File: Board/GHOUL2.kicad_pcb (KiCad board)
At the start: 2 copper layers, 106.7 x 73.7 mm, 16 parts, among them J1 Conn_01x02, Q1 IRF540N, Q2 IRF540N, U1 Teensy3.5_All_Pins, U10 GHOULIMU, U2 LM7805_TO220, U3 BMP280, U4 Feedback_Serv, U5 LM1084-ADJ, U6 NichromeConnector, U7 Ultimate_GPS_Breakout_v3, U8 Xbee, U9 NichromeConnector

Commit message: sometimes the fastest way to get to the end is to throw everything out and start over
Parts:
- R1, U5: moved to F.Cu
- moved Q2 33.7 mm to (189.7, 91.2), turned to 0 degrees
- moved U6 18.8 mm to (195.8, 106.4), turned to 90 degrees
- moved C1 16.1 mm to (165.0, 68.7), turned to 180 degrees
- moved R1 15.3 mm to (181.3, 116.8), turned to 180 degrees
- moved U5 15.3 mm to (181.3, 104.1), turned to 180 degrees
- moved U2 12.4 mm to (176.2, 77.9), turned to -90 degrees
- moved U4 10.2 mm to (105.5, 76.1)
- moved U1 8.03 mm to (160.0, 106.7)
- moved U9 7.16 mm to (195.8, 116.6), turned to -90 degrees
- moved Q1 6.61 mm to (189.7, 129.3), turned to 0 degrees
- moved BT1 3.59 mm to (139.7, 129.5)
- moved U8 3.59 mm to (128.8, 135.8)
- moved J1 2.71 mm to (185.8, 73.7)
- moved U7 2.54 mm to (128.7, 104.0)
- moved U10 2.54 mm to (148.5, 91.3)
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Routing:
- net GND: track 235.9 -> 0.00 mm, vias 3 -> 0
- net 5v pwr: track 182.4 -> 8.24 mm, vias 1 -> 0
- net Net-(U1-Pad22): track 73.0 -> 0.00 mm
- net Nic2: track 68.7 -> 0.00 mm, vias 1 -> 0
- net Net-(U1-Pad2): track 67.0 -> 0.00 mm
- net Net-(U1-Pad3): track 57.7 -> 0.00 mm
- net Nic1: track 51.6 -> 0.00 mm
- net Feedback: track 50.1 -> 0.00 mm
- net Net-(U1-Pad12): track 48.9 -> 0.00 mm
- net Net-(U1-Pad51): track 44.9 -> 0.00 mm, vias 1 -> 0
- net Net-(U1-Pad9): track 41.5 -> 0.00 mm
- net Net-(U1-Pad10): track 34.6 -> 0.00 mm
- net Vin: track 29.0 -> 60.9 mm, vias 0 -> 5
- net Net-(U1-Pad11): track 27.4 -> 0.00 mm
- net Net-(BT1-Pad1): track 14.8 -> 0.00 mm
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- removed copper zone on F.Cu, net GND
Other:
- board size 106.7 x 73.7 mm -> 105.1 x 68.6 mm

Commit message: fixed some routing
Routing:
- net Net-(R1-Pad1): track 30.3 -> 36.1 mm
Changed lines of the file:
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@@
   (segment (start 195.81 103.905) (end 195.81 93.975) (width 2) (layer "F.Cu") (net 24))
   (segment (start 195.81 93.975) (end 193.04 91.205) (width 0.25) (layer "F.Cu") (net 24))
+  (segment (start 189.84 116.605) (end 195.81 116.605) (width 2) (layer "F.Cu") (net 25))
   (segment (start 195.81 110.635) (end 195.81 106.405) (width 2) (layer "F.Cu") (net 25))
   (segment (start 195.58 116.605) (end 195.81 116.605) (width 2) (layer "F.Cu") (net 25))
-  (segment (start 192.71 113.735) (end 195.58 116.605) (width 2) (layer "F.Cu") (net 25))
   (segment (start 187.065 106.68) (end 187.065 108.09) (width 2) (layer "F.Cu") (net 25))
   (segment (start 187.065 108.09) (end 192.71 113.735) (width 2) (layer "F.Cu") (net 25))
+  (segment (start 187.065 119.38) (end 192.71 113.735) (width 2) (layer "F.Cu") (net 25))
+  (segment (start 187.065 119.38) (end 189.84 116.605) (width 2) (layer "F.Cu") (net 25))
   (segment (start 192.71 113.735) (end 195.81 110.635) (width 2) (layer "F.Cu") (net 25))
-  (segment (start 187.065 119.38) (end 192.71 113.735) (width 2) (layer "F.Cu") (net 25))
   (segment (start 173.67 72.13) (end 172.98 72.13) (width 1) (layer "F.Cu") (net 45))
   (segment (start 172.98 72.13) (end 167.64 77.47) (width 1) (layer "F.Cu") (net 45))

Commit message: progress
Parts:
- moved U1 2.54 mm to (160.0, 104.1)
- moved U6 2.27 mm to (195.8, 104.1)
- moved U2 0.95 mm to (175.3, 77.9)
- moved U9 0.47 mm to (195.8, 117.1), turned to 90 degrees
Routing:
- net Vin: track 60.9 -> 88.7 mm, vias 5 -> 9
- net Net-(R1-Pad1): track 36.1 -> 33.0 mm
- net Net-(Q2-Pad2): track 13.8 -> 11.6 mm
- net 5v pwr: track 8.24 -> 6.39 mm
- net Net-(Q1-Pad2): track 11.7 -> 13.4 mm
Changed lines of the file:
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@@
   )
   (footprint "teensy:Teensy35_36_All_Pins" (layer "F.Cu")
-    (at 160.02 106.68 -90)
+    (at 160.02 104.14 -90)
     (property "Pinouts" "https://www.pjrc.com/teensy/pinout.html")
     (property "Sheetfile" "GHOUL2.kicad_sch")
@@
   )
   (footprint "Package_TO_SOT_SMD:TO-263-3_TabPin2" (layer "F.Cu")
-    (at 176.21 77.905 -90)
+    (at 175.26 77.905 -90)
     (descr "TO-263 / D2PAK / DDPAK SMD package, http://www.infineon.com/cms/en/product/packages/PG-TO263/PG-TO263-3-1/")
     (tags "D2PAK DDPAK TO-263 D2PAK-3 TO-263-3 SOT-404")
@@
   )
   (footprint "Connector_JST:JST_EH_B2B-EH-A_1x02_P2.50mm_Vertical" (layer "F.Cu")
-    (at 195.81 106.405 90)
+    (at 195.81 104.14 90)
     (descr "JST EH series connector, B2B-EH-A (http://www.jst-mfg.com/product/pdf/eng/eEH.pdf), generated with kicad-footprint-generator")
     (tags "connector JST EH vertical")
@@
   )
   (footprint "Connector_JST:JST_EH_B2B-EH-A_1x02_P2.50mm_Vertical" (layer "F.Cu")
-    (at 195.81 116.605 -90)
+    (at 195.81 117.075 90)
     (descr "JST EH series connector, B2B-EH-A (http://www.jst-mfg.com/product/pdf/eng/eEH.pdf), generated with kicad-footprint-generator")
     (tags "connector JST EH vertical")
@@
     (fp_line (start -2.5 -1.6) (end -2.5 2.2) (layer "F.Fab") (width 0.1))
     (fp_line (start -2.91 0.11) (end -2.91 2.61) (layer "F.Fab") (width 0.1))
-    (pad "1" thru_hole roundrect (at 0 0 270) (size 1.7 2) (drill 1) (layers *.Cu *.Mask) (roundrect_rratio 0.147059)
+    (pad "1" thru_hole oval (at 2.5 0 90) (size 1.7 2) (drill 1) (layers *.Cu *.Mask)
       (net 25 "Net-(R1-Pad1)") (pinfunction "In") (pintype "input"))
-    (pad "2" thru_hole oval (at 2.5 0 270) (size 1.7 2) (drill 1) (layers *.Cu *.Mask)
+    (pad "2" thru_hole roundrect (at 0 0 90) (size 1.7 2) (drill 1) (layers *.Cu *.Mask) (roundrect_rratio 0.147059)
       (net 16 "Net-(Q1-Pad2)") (pinfunction "Out") (pintype "input"))
     (model "${KICAD6_3DMODEL_DIR}/Connector_JST.3dshapes/JST_EH_B2B-EH-A_1x02_P2.50mm_Vertical.wrl"
@@
   (gr_line (start 93.98 137.16) (end 99.06 137.16) (layer "Edge.Cuts") (width 0.1))
   (gr_line (start 93.98 68.58) (end 93.98 137.16) (layer "Edge.Cuts") (width 0.1))
-  (segment (start 195.81 119.105) (end 195.81 126.53) (width 2) (layer "F.Cu") (net 16))
-  (segment (start 195.535 119.38) (end 195.81 119.105) (width 0.25) (layer "F.Cu") (net 16))
-  (segment (start 195.81 126.53) (end 193.035 129.305) (width 2) (layer "F.Cu") (net 16))
-  (segment (start 195.81 103.905) (end 195.81 93.975) (width 2) (layer "F.Cu") (net 24))
+  (segment (start 195.81 117.075) (end 193.035 119.85) (width 2) (layer "F.Cu") (net 16))
+  (segment (start 193.035 119.85) (end 193.035 129.305) (width 2) (layer "F.Cu") (net 16))
+  (segment (start 195.81 101.64) (end 195.81 93.975) (width 2) (layer "F.Cu") (net 24))
   (segment (start 195.81 93.975) (end 193.04 91.205) (width 0.25) (layer "F.Cu") (net 24))
-  (segment (start 189.84 116.605) (end 195.81 116.605) (width 2) (layer "F.Cu") (net 25))
-  (segment (start 195.81 110.635) (end 195.81 106.405) (width 2) (layer "F.Cu") (net 25))
-  (segment (start 195.58 116.605) (end 195.81 116.605) (width 2) (layer "F.Cu") (net 25))
-  (segment (start 187.065 106.68) (end 187.065 108.09) (width 2) (layer "F.Cu") (net 25))
-  (segment (start 187.065 108.09) (end 192.71 113.735) (width 2) (layer "F.Cu") (net 25))
-  (segment (start 187.065 119.38) (end 192.71 113.735) (width 2) (layer "F.Cu") (net 25))
-  (segment (start 187.065 119.38) (end 189.84 116.605) (width 2) (layer "F.Cu") (net 25))
+  (segment (start 187.065 119.38) (end 191.3225 115.1225) (width 2) (layer "F.Cu") (net 25))
+  (segment (start 195.81 110.635) (end 195.81 104.14) (width 2) (layer "F.Cu") (net 25))
+  (segment (start 187.065 106.68) (end 187.065 108.09) (width 1) (layer "F.Cu") (net 25))
   (segment (start 192.71 113.735) (end 195.81 110.635) (width 2) (layer "F.Cu") (net 25))
-  (segment (start 173.67 72.13) (end 172.98 72.13) (width 1) (layer "F.Cu") (net 45))
-  (segment (start 172.98 72.13) (end 167.64 77.47) (width 1) (layer "F.Cu") (net 45))
-  (segment (start 191.45 101.6) (end 187.065 101.6) (width 2) (layer "F.Cu") (net 101))
+  (segment (start 187.065 108.09) (end 192.71 113.735) (width 1) (layer "F.Cu") (net 25))
+  (segment (start 191.87 114.575) (end 191.3225 115.1225) (width 0.25) (layer "F.Cu") (net 25))
+  (segment (start 195.81 114.575) (end 191.87 114.575) (width 2) (layer "F.Cu") (net 25))
+  (segment (start 191.3225 115.1225) (end 192.71 113.735) (width 2) (layer "F.Cu") (net 25))
+  (segment (start 172.72 72.13) (end 172.72 72.39) (width 1) (layer "F.Cu") (net 45))
+  (segment (start 172.72 72.39) (end 170.18 74.93) (width 1) (layer "F.Cu") (net 45))
+  (segment (start 170.18 74.93) (end 167.64 74.93) (width 1) (layer "F.Cu") (net 45))
+  (segment (start 190.5 101.6) (end 187.065 101.6) (width 2) (layer "F.Cu") (net 101))
+  (segment (start 191.45 101.6) (end 190.5 101.6) (width 2) (layer "F.Cu") (net 101))
   (segment (start 185.775 78.7) (end 185.38 78.7) (width 2) (layer "F.Cu") (net 101))
-  (segment (start 186.37 99.06) (end 191.45 99.06) (width 2) (layer "F.Cu") (net 101))
+  (segment (start 186.37 99.06) (end 187.96 99.06) (width 2) (layer "F.Cu") (net 101))
   (segment (start 185.775 97.115) (end 185.775 98.465) (width 2) (layer "F.Cu") (net 101))
-  (segment (start 178.81 72.13) (end 178.75 72.13) (width 1) (layer "F.Cu") (net 101))
+  (segment (start 186.965 97.115) (end 187.165 97.315) (width 2) (layer "F.Cu") (net 101))
+  (segment (start 178.81 72.13) (end 177.8 72.13) (width 1) (layer "F.Cu") (net 101))
+  (segment (start 185.38 78.7) (end 178.81 72.13) (width 1) (layer "F.Cu") (net 101))
   (segment (start 190.755 101.6) (end 188.91 99.755) (width 2) (layer "F.Cu") (net 101))
-  (segment (start 191.45 99.06) (end 191.45 101.6) (width 2) (layer "F.Cu") (net 101))
+  (segment (start 187.96 99.06) (end 190.5 99.06) (width 2) (layer "F.Cu") (net 101))
+  (segment (start 191.45 101.6) (end 191.45 99.06) (width 2) (layer "F.Cu") (net 101))
   (segment (start 186.37 100.905) (end 187.065 101.6) (width 2) (layer "F.Cu") (net 101))
+  (segment (start 187.165 97.315) (end 188.91 99.06) (width 2) (layer "F.Cu") (net 101))
   (segment (start 191.45 101.6) (end 190.755 101.6) (width 2) (layer "F.Cu") (net 101))
   (segment (start 188.91 99.06) (end 188.91 99.755) (width 2) (layer "F.Cu") (net 101))
+  (segment (start 185.775 97.115) (end 186.965 97.115) (width 2) (layer "F.Cu") (net 101))
   (segment (start 186.37 99.06) (end 186.37 100.905) (width 2) (layer "F.Cu") (net 101))
   (segment (start 188.91 99.755) (end 187.065 101.6) (width 2) (layer "F.Cu") (net 101))
   (segment (start 191.45 99.06) (end 189.605 99.06) (width 2) (layer "F.Cu") (net 101))
-  (segment (start 185.38 78.7) (end 178.81 72.13) (width 1) (layer "F.Cu") (net 101))
+  (segment (start 190.5 99.06) (end 191.45 99.06) (width 2) (layer "F.Cu") (net 101))
   (segment (start 185.775 98.465) (end 186.37 99.06) (width 2) (layer "F.Cu") (net 101))
   (via (at 191.45 99.06) (size 0.8) (drill 0.4) (layers "F.Cu" "B.Cu") (net 101))
@@
   (via (at 185.775 97.115) (size 0.8) (drill 0.4) (layers "F.Cu" "B.Cu") (net 101))
   (via (at 191.45 101.6) (size 0.8) (drill 0.4) (layers "F.Cu" "B.Cu") (net 101))
+  (via (at 190.5 101.6) (size 0.8) (drill 0.4) (layers "F.Cu" "B.Cu") (net 101))
+  (via (at 187.96 99.06) (size 0.8) (drill 0.4) (layers "F.Cu" "B.Cu") (net 101))
+  (via (at 187.165 97.315) (size 0.8) (drill 0.4) (layers "F.Cu" "B.Cu") (net 101))
   (via (at 188.91 99.06) (size 0.8) (drill 0.4) (layers "F.Cu" "B.Cu") (net 101))
+  (via (at 190.5 99.06) (size 0.8) (drill 0.4) (layers "F.Cu" "B.Cu") (net 101))
   (segment (start 186.37 99.06) (end 188.91 99.06) (width 2) (layer "B.Cu") (net 101))
+  (segment (start 187.32 99.06) (end 188.91 100.65) (width 2) (layer "B.Cu") (net 101))
+  (segment (start 186.37 99.06) (end 187.32 99.06) (width 2) (layer "B.Cu") (net 101))
+  (segment (start 188.91 99.06) (end 188.91 100.65) (width 2) (layer "B.Cu") (net 101))
   (segment (start 185.775 78.7) (end 185.775 97.115) (width 2) (layer "B.Cu") (net 101))
+  (segment (start 187.96 101.6) (end 191.45 101.6) (width 2) (layer "B.Cu") (net 101))
   (segment (start 188.91 99.06) (end 191.45 99.06) (width 2) (layer "B.Cu") (net 101))
   (segment (start 185.775 97.115) (end 185.775 98.465) (width 2) (layer "B.Cu") (net 101))
+  (segment (start 188.91 100.65) (end 187.96 101.6) (width 2) (layer "B.Cu") (net 101))
+  (segment (start 185.775 97.115) (end 186.965 97.115) (width 2) (layer "B.Cu") (net 101))
+  (segment (start 186.37 99.06) (end 186.37 100.01) (width 2) (layer "B.Cu") (net 101))
+  (segment (start 186.37 100.01) (end 187.96 101.6) (width 2) (layer "B.Cu") (net 101))
+  (segment (start 191.45 99.06) (end 191.45 101.6) (width 2) (layer "B.Cu") (net 101))
+  (segment (start 186.965 97.115) (end 191.45 101.6) (width 2) (layer "B.Cu") (net 101))
   (segment (start 185.775 98.465) (end 186.37 99.06) (width 2) (layer "B.Cu") (net 101))
   (segment (start 177.915 104.14) (end 187.065 113.29) (width 2) (layer "F.Cu") (net 102))

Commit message: lots of improvements
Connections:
- net Net-(U1-Pad10) renamed SDA
- net Net-(U1-Pad9) renamed SCL
- U1 pad 15: unconnected-(U1-Pad15) -> 3v3 pwr
- U1 pad 18: unconnected-(U1-Pad18) -> Xbee DIn
- U1 pad 19: unconnected-(U1-Pad19) -> Xbee DOut
- U1 pad 2: Net-(U1-Pad2) -> unconnected-(U1-Pad2)
- U1 pad 22: Net-(U1-Pad22) -> unconnected-(U1-Pad22)
- U1 pad 3: Net-(U1-Pad3) -> unconnected-(U1-Pad3)
- U1 pad 32: unconnected-(U1-Pad32) -> Nic2
- U1 pad 33: unconnected-(U1-Pad33) -> Nic1
- U1 pad 4: Nic2 -> Servo PWM
- U1 pad 51: Net-(U1-Pad51) -> unconnected-(U1-Pad51)
- U1 pad 8: Nic1 -> unconnected-(U1-Pad8)
- U10 pad 1: Net-(U1-Pad51) -> 3v3 pwr
- U4 pad 1: Net-(U1-Pad22) -> Servo PWM
- U8 pad 3: Net-(U1-Pad2) -> Xbee DOut
- U8 pad 4: Net-(U1-Pad3) -> Xbee DIn
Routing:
- net 5v pwr: track 6.39 -> 108.4 mm
- net Servo PWM: track 0.00 -> 61.7 mm
- net Feedback: track 0.00 -> 57.8 mm
- net Net-(U1-Pad11): track 0.00 -> 48.5 mm
- net Nic1: track 0.00 -> 44.8 mm
- net Net-(U1-Pad12): track 0.00 -> 42.3 mm
- net Net-(U1-Pad25): track 0.00 -> 41.5 mm
- net 3v3 pwr: track 0.00 -> 26.0 mm
- net Xbee DIn: track 0.00 -> 25.8 mm
- net Xbee DOut: track 0.00 -> 25.1 mm
- net Nic2: track 0.00 -> 16.9 mm

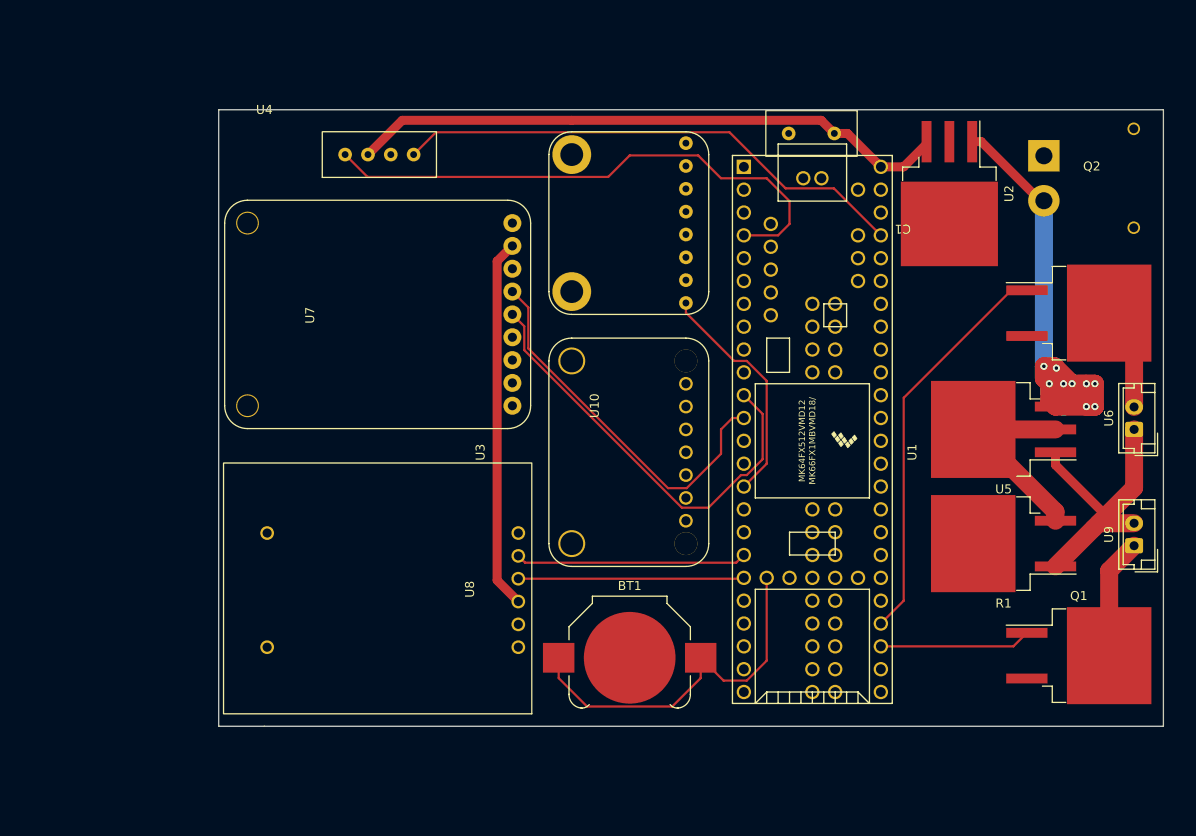
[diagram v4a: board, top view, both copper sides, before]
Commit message: finished layout for pcb v2 first draft
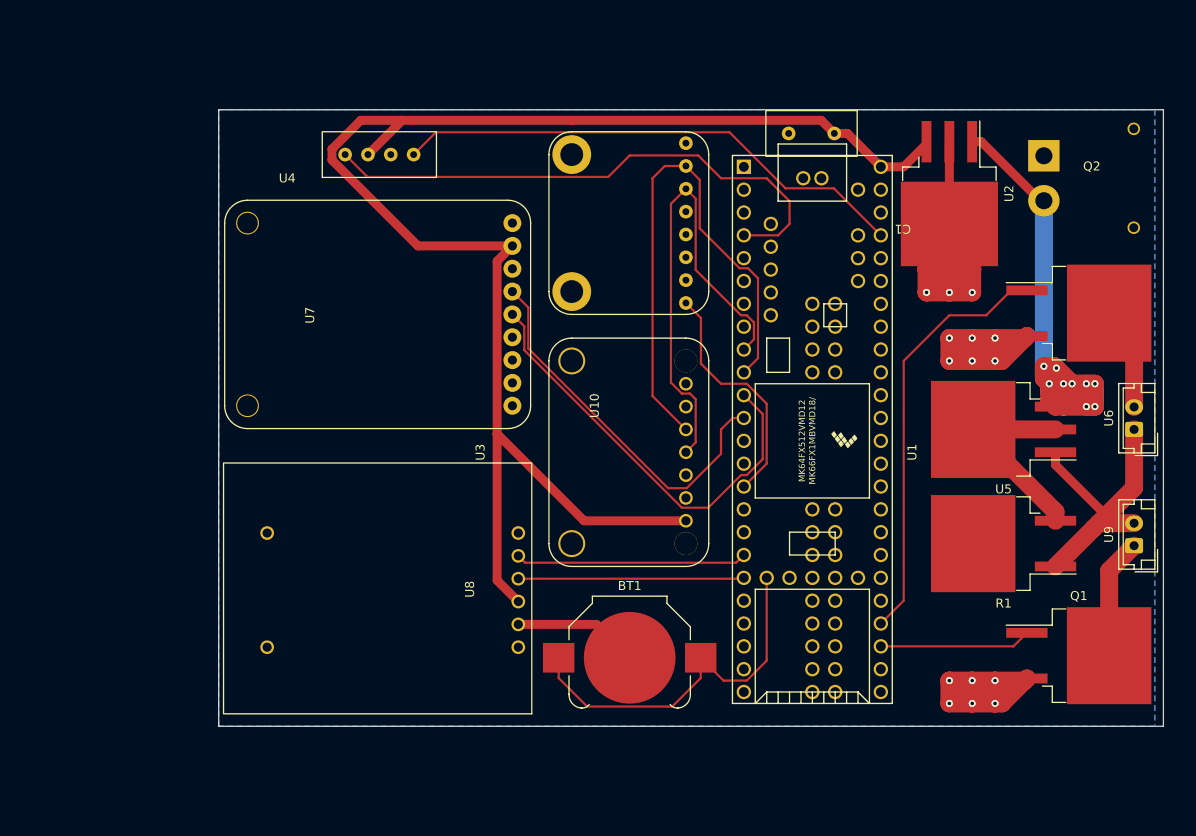
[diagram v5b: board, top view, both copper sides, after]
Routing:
- net GND: track 0.00 -> 136.6 mm, vias 0 -> 15
- net SDA: track 0.00 -> 61.2 mm
- net 5v pwr: track 108.4 -> 167.8 mm
- net SCL: track 0.00 -> 54.0 mm
- net Nic1: track 44.8 -> 47.2 mm
- net 3v3 pwr: track 26.0 -> 26.9 mm
- added copper zone on B.Cu, net GND

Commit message: made it way more complicated, in a good way?
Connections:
- R1 pad 2: (no net) -> GND
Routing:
- net Net-(R1-Pad1): track 33.0 -> 5.97 mm
- net Net-(R1-Pad3): track 23.1 -> 9.15 mm
- net Net-(Q1-Pad2): track 13.4 -> 0.00 mm
- net Servo PWM: track 61.7 -> 52.3 mm
- net Net-(Q2-Pad2): track 11.6 -> 3.92 mm
- net GND: track 136.6 -> 129.5 mm, vias 15 -> 28
- net 5v pwr: track 167.8 -> 171.1 mm
- net Vin: track 88.7 -> 91.1 mm, vias 9 -> 8
- net SDA: track 61.2 -> 59.0 mm
- added copper zone on F.Cu, net Net-(Q1-Pad2)
- added copper zone on F.Cu, net Net-(Q2-Pad2)
- added copper zone on F.Cu, net Net-(R1-Pad1)
- added copper zone on F.Cu, net Net-(R1-Pad3)
